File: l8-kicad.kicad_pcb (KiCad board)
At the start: 4 copper layers, 55.5 x 89.5 mm, 97 parts, among them J1 USB_B_Mini, J2 LCD 3.2" 240x320 Conn_01x14_P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, J3 Screw_Terminal_01x06, J4 Conn_ST_STDC14, J7 TC2030 - TAG Connect, Q1 SI2301CDS-T1-GE3, Q4 SI2301CDS-T1-GE3, Q5 SI2301CDS-T1-GE3, SW1 SW_Push, SW2 SW_Push, U1 B0505S-1WR2, U2 ISO1042-Q1, U22 TLV76733DRVx, U3 STM32F427V_G-I_Tx, U4 ST_SENSOR_2, U5 IIS3DHHCTR, X1 8MHz 20pF

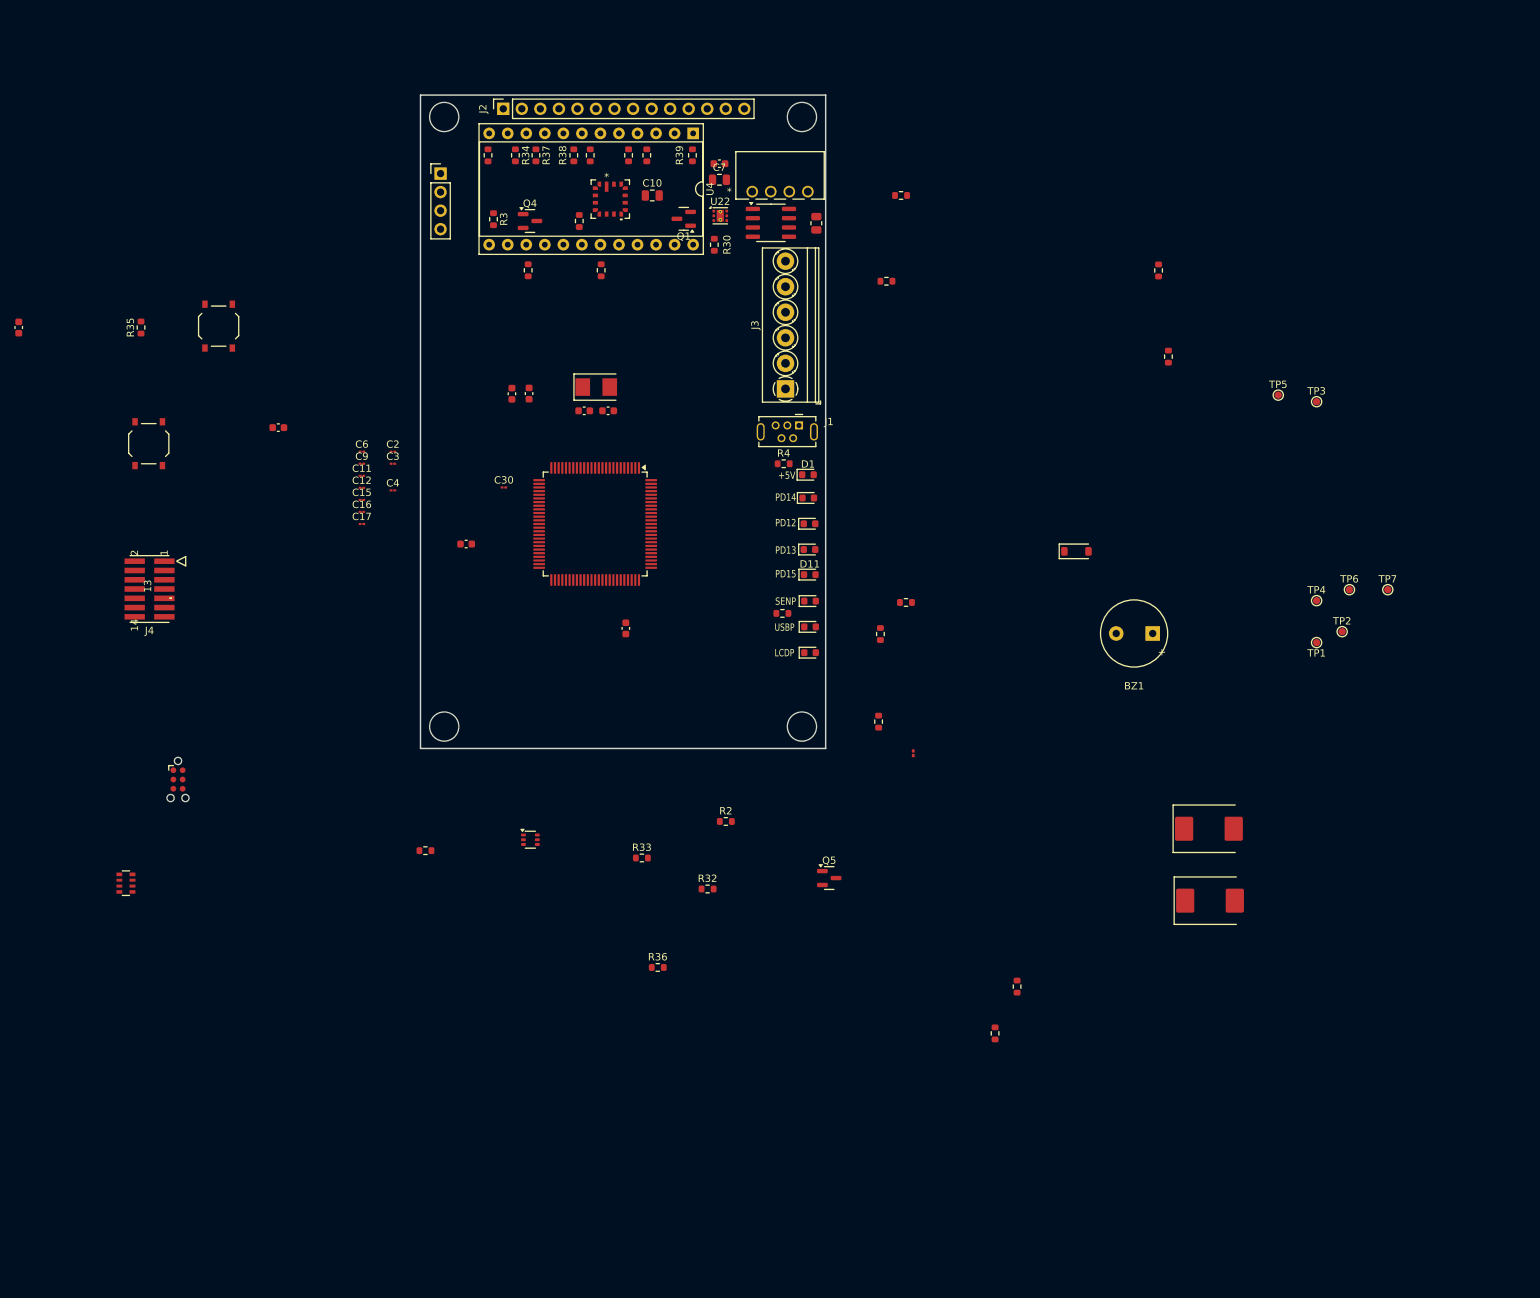
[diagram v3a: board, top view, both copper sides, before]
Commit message: add tp  move leds +
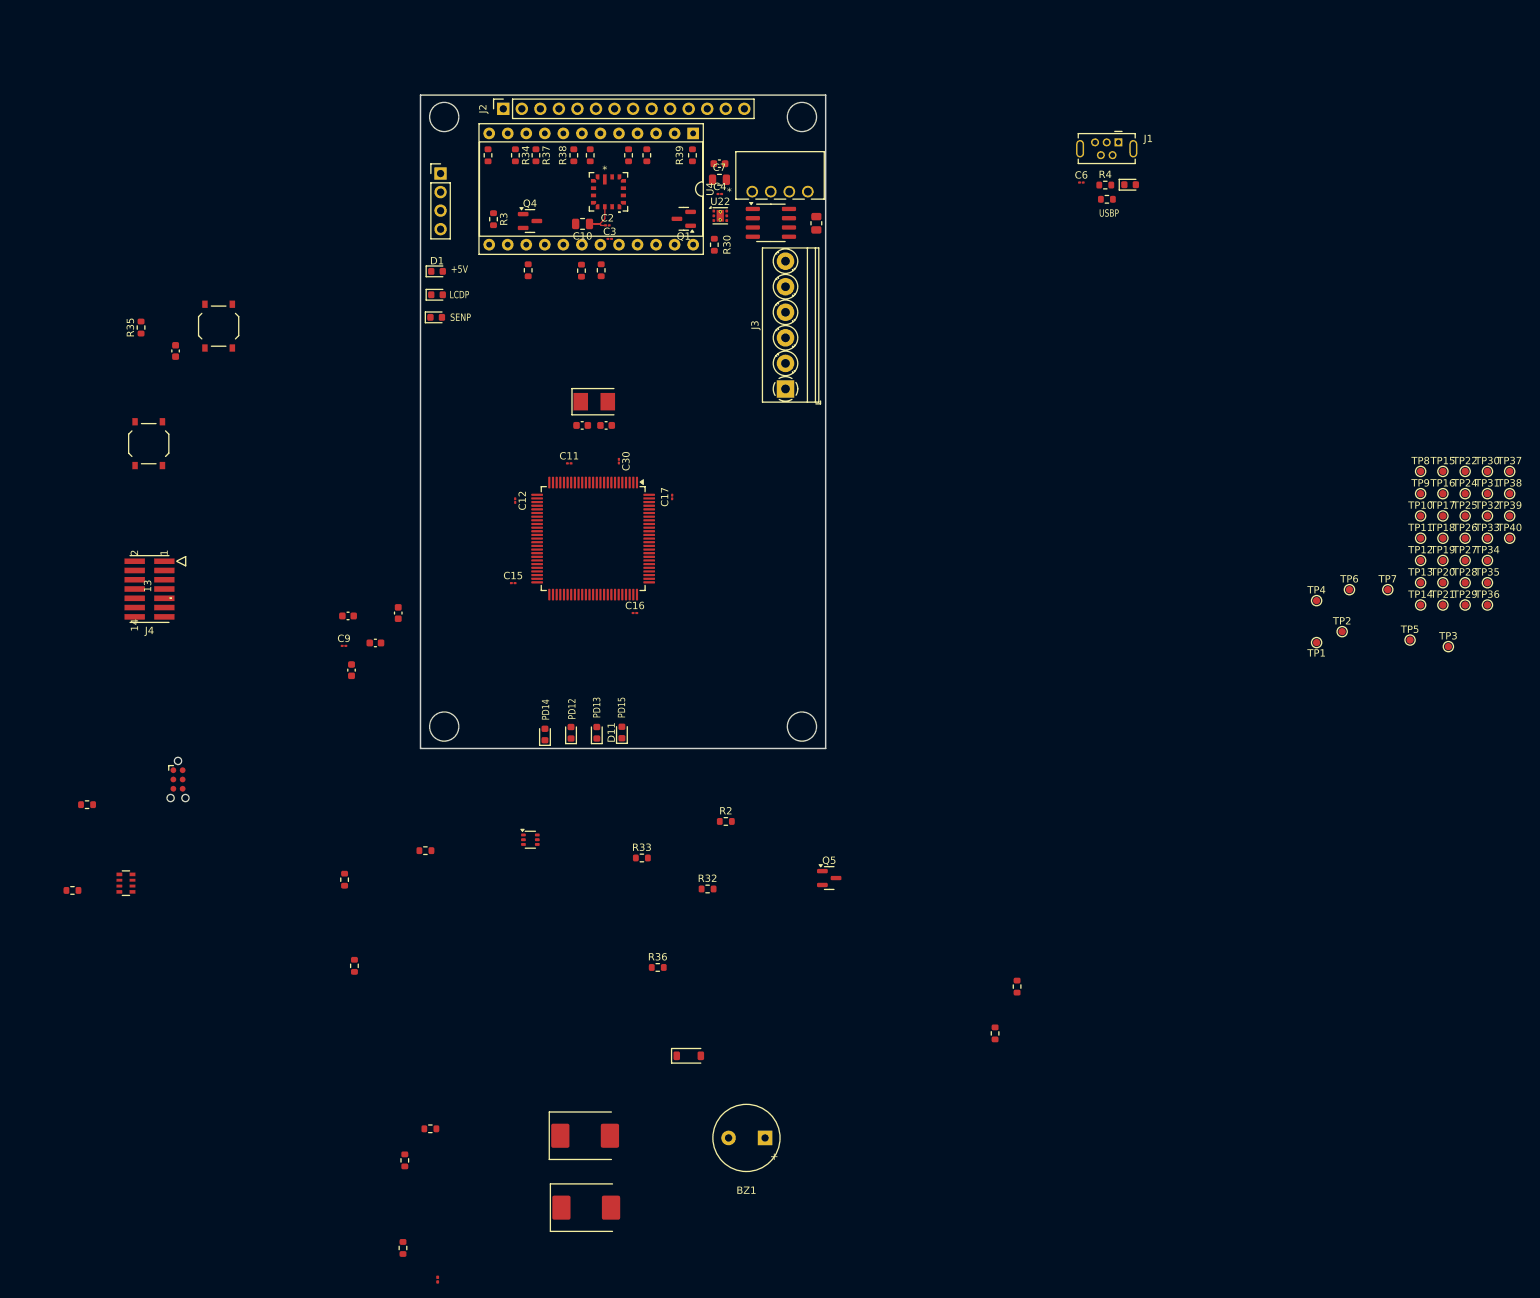
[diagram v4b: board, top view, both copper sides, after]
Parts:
- removed C27: 1uF, Capacitor_SMD:C_0603_1608Metric
- added TP10: PC8, TestPoint:TestPoint_Pad_D1.0mm, F.Cu at (237.0, 157.7)
- added TP11: PC9, TestPoint:TestPoint_Pad_D1.0mm, F.Cu at (237.0, 160.7)
- added TP12: PC13, TestPoint:TestPoint_Pad_D1.0mm, F.Cu at (237.0, 163.8)
- added TP13: PC14, TestPoint:TestPoint_Pad_D1.0mm, F.Cu at (237.0, 166.8)
- added TP14: PC15, TestPoint:TestPoint_Pad_D1.0mm, F.Cu at (237.0, 169.8)
- added TP15: PC0, TestPoint:TestPoint_Pad_D1.0mm, F.Cu at (240.1, 151.6)
- added TP16: PA0, TestPoint:TestPoint_Pad_D1.0mm, F.Cu at (240.1, 154.6)
- added TP17: PA1, TestPoint:TestPoint_Pad_D1.0mm, F.Cu at (240.1, 157.7)
- added TP18: PA4, TestPoint:TestPoint_Pad_D1.0mm, F.Cu at (240.1, 160.7)
- added TP19: PA8, TestPoint:TestPoint_Pad_D1.0mm, F.Cu at (240.1, 163.8)
- added TP20: PB4, TestPoint:TestPoint_Pad_D1.0mm, F.Cu at (240.1, 166.8)
- added TP21: PB5, TestPoint:TestPoint_Pad_D1.0mm, F.Cu at (240.1, 169.8)
- added TP22: PB8, TestPoint:TestPoint_Pad_D1.0mm, F.Cu at (243.1, 151.6)
- added TP24: PB10, TestPoint:TestPoint_Pad_D1.0mm, F.Cu at (243.1, 154.6)
- added TP25: PB11, TestPoint:TestPoint_Pad_D1.0mm, F.Cu at (243.1, 157.7)
- added TP26: PB12, TestPoint:TestPoint_Pad_D1.0mm, F.Cu at (243.1, 160.7)
- added TP27: PD6, TestPoint:TestPoint_Pad_D1.0mm, F.Cu at (243.1, 163.8)
- added TP28: PD7, TestPoint:TestPoint_Pad_D1.0mm, F.Cu at (243.1, 166.8)
- added TP29: PD8, TestPoint:TestPoint_Pad_D1.0mm, F.Cu at (243.1, 169.8)
- added TP30: PD9, TestPoint:TestPoint_Pad_D1.0mm, F.Cu at (246.2, 151.6)
- added TP31: PE8, TestPoint:TestPoint_Pad_D1.0mm, F.Cu at (246.2, 154.6)
- added TP32: PE7, TestPoint:TestPoint_Pad_D1.0mm, F.Cu at (246.2, 157.7)
- added TP33: PE0, TestPoint:TestPoint_Pad_D1.0mm, F.Cu at (246.2, 160.7)
- added TP34: PE1, TestPoint:TestPoint_Pad_D1.0mm, F.Cu at (246.2, 163.8)
- added TP35: PE9, TestPoint:TestPoint_Pad_D1.0mm, F.Cu at (246.2, 166.8)
- added TP36: PE10, TestPoint:TestPoint_Pad_D1.0mm, F.Cu at (246.2, 169.8)
- added TP37: PE11, TestPoint:TestPoint_Pad_D1.0mm, F.Cu at (249.2, 151.6)
- added TP38: PE12, TestPoint:TestPoint_Pad_D1.0mm, F.Cu at (249.2, 154.6)
- added TP39: PD10, TestPoint:TestPoint_Pad_D1.0mm, F.Cu at (249.2, 157.7)
- added TP40: PD11, TestPoint:TestPoint_Pad_D1.0mm, F.Cu at (249.2, 160.7)
- added TP8: PC6, TestPoint:TestPoint_Pad_D1.0mm, F.Cu at (237.0, 151.6)
- added TP9: PC7, TestPoint:TestPoint_Pad_D1.0mm, F.Cu at (237.0, 154.6)
- moved R13 139.3 mm to (91.0, 219.3)
- moved R45 139.3 mm to (52.3, 208.9)
- moved R47 139.3 mm to (54.3, 197.2)
- moved R5 139.3 mm to (89.6, 207.5)
- moved C6 105.2 mm to (190.5, 112.0)
- moved R43 97.2 mm to (97.8, 245.9)
- moved R8 97.2 mm to (97.6, 257.9)
- moved FB1 97.2 mm to (102.3, 262.3)
- moved R6 97.2 mm to (101.3, 241.6)
- moved D2 95.2 mm to (122.5, 242.6)
- moved D3 95.2 mm to (122.7, 252.4)
- moved BZ1 87.1 mm to (148.4, 242.8)
- moved D17 87.1 mm to (136.8, 231.6)
- moved D10 74.8 mm to (197.2, 112.3)
- moved R48 72.1 mm to (194.0, 114.3)
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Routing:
- net +3.3V: track 0.00 -> 5.73 mm

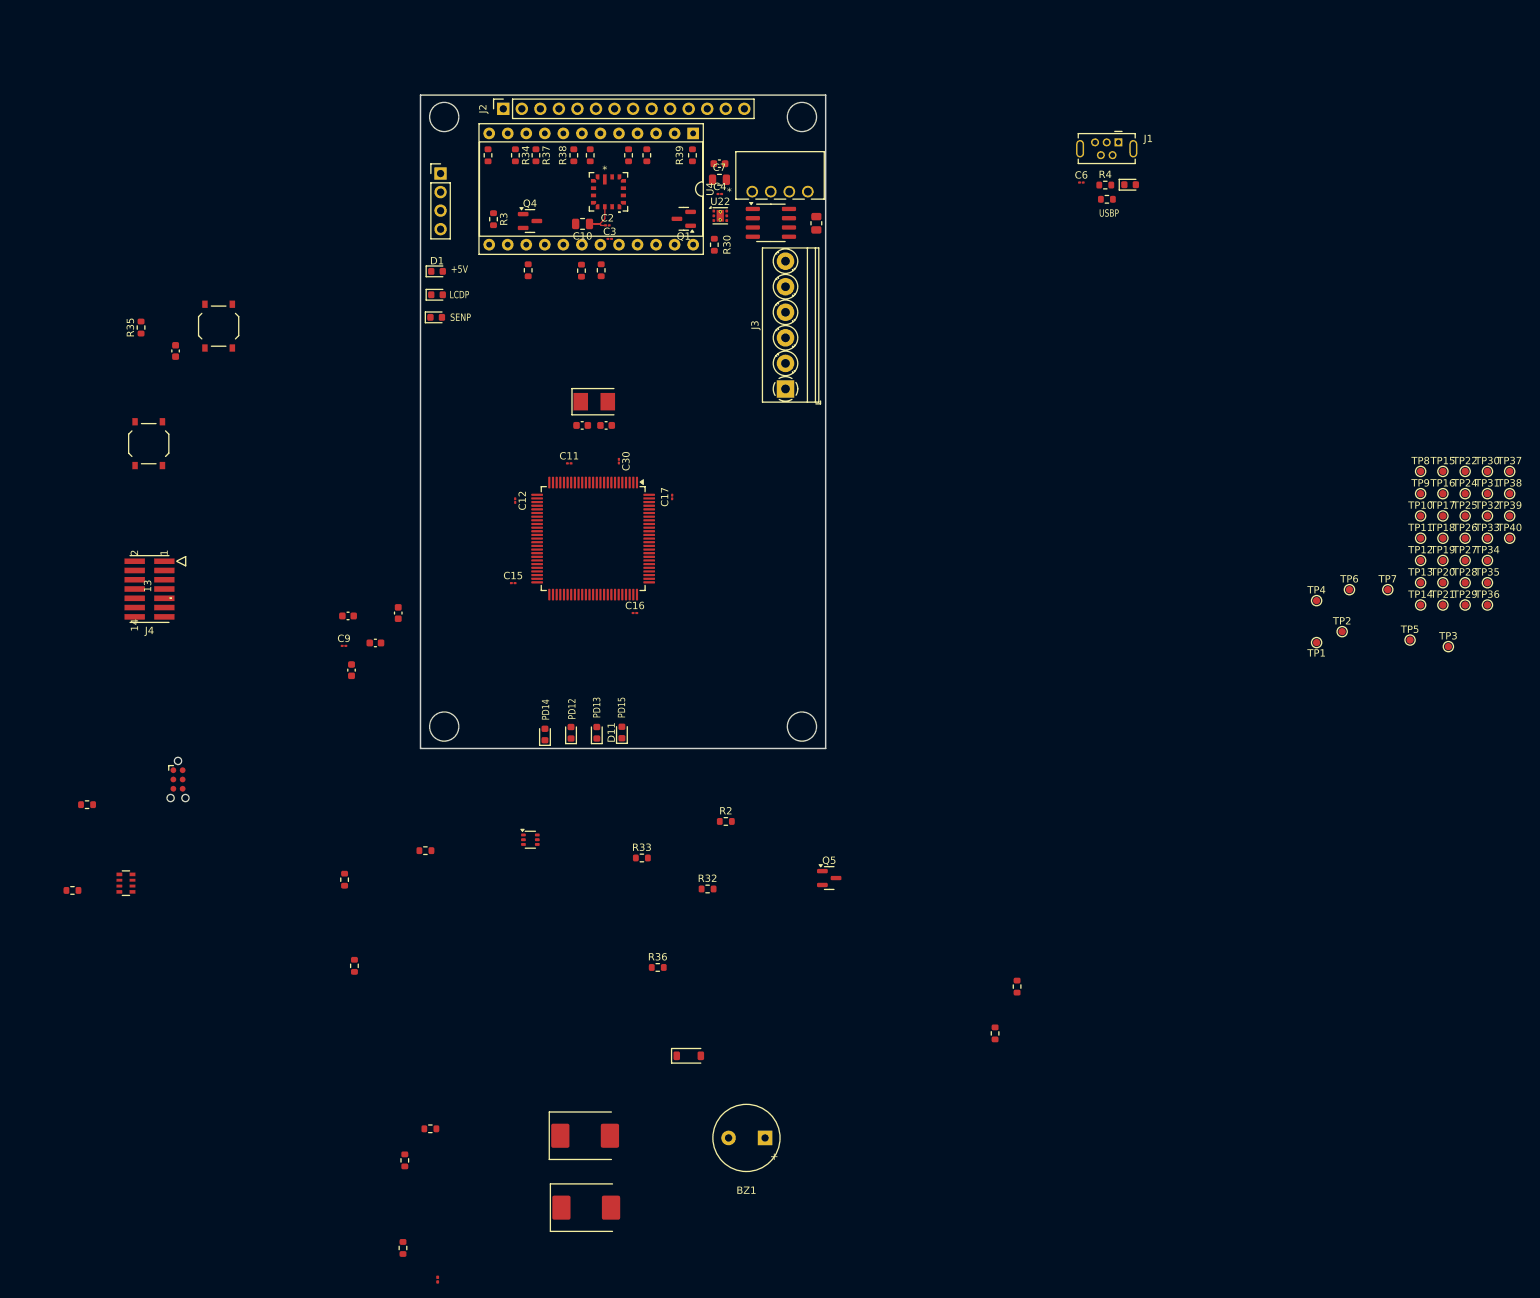
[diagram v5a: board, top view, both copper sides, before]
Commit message: smaller test pads
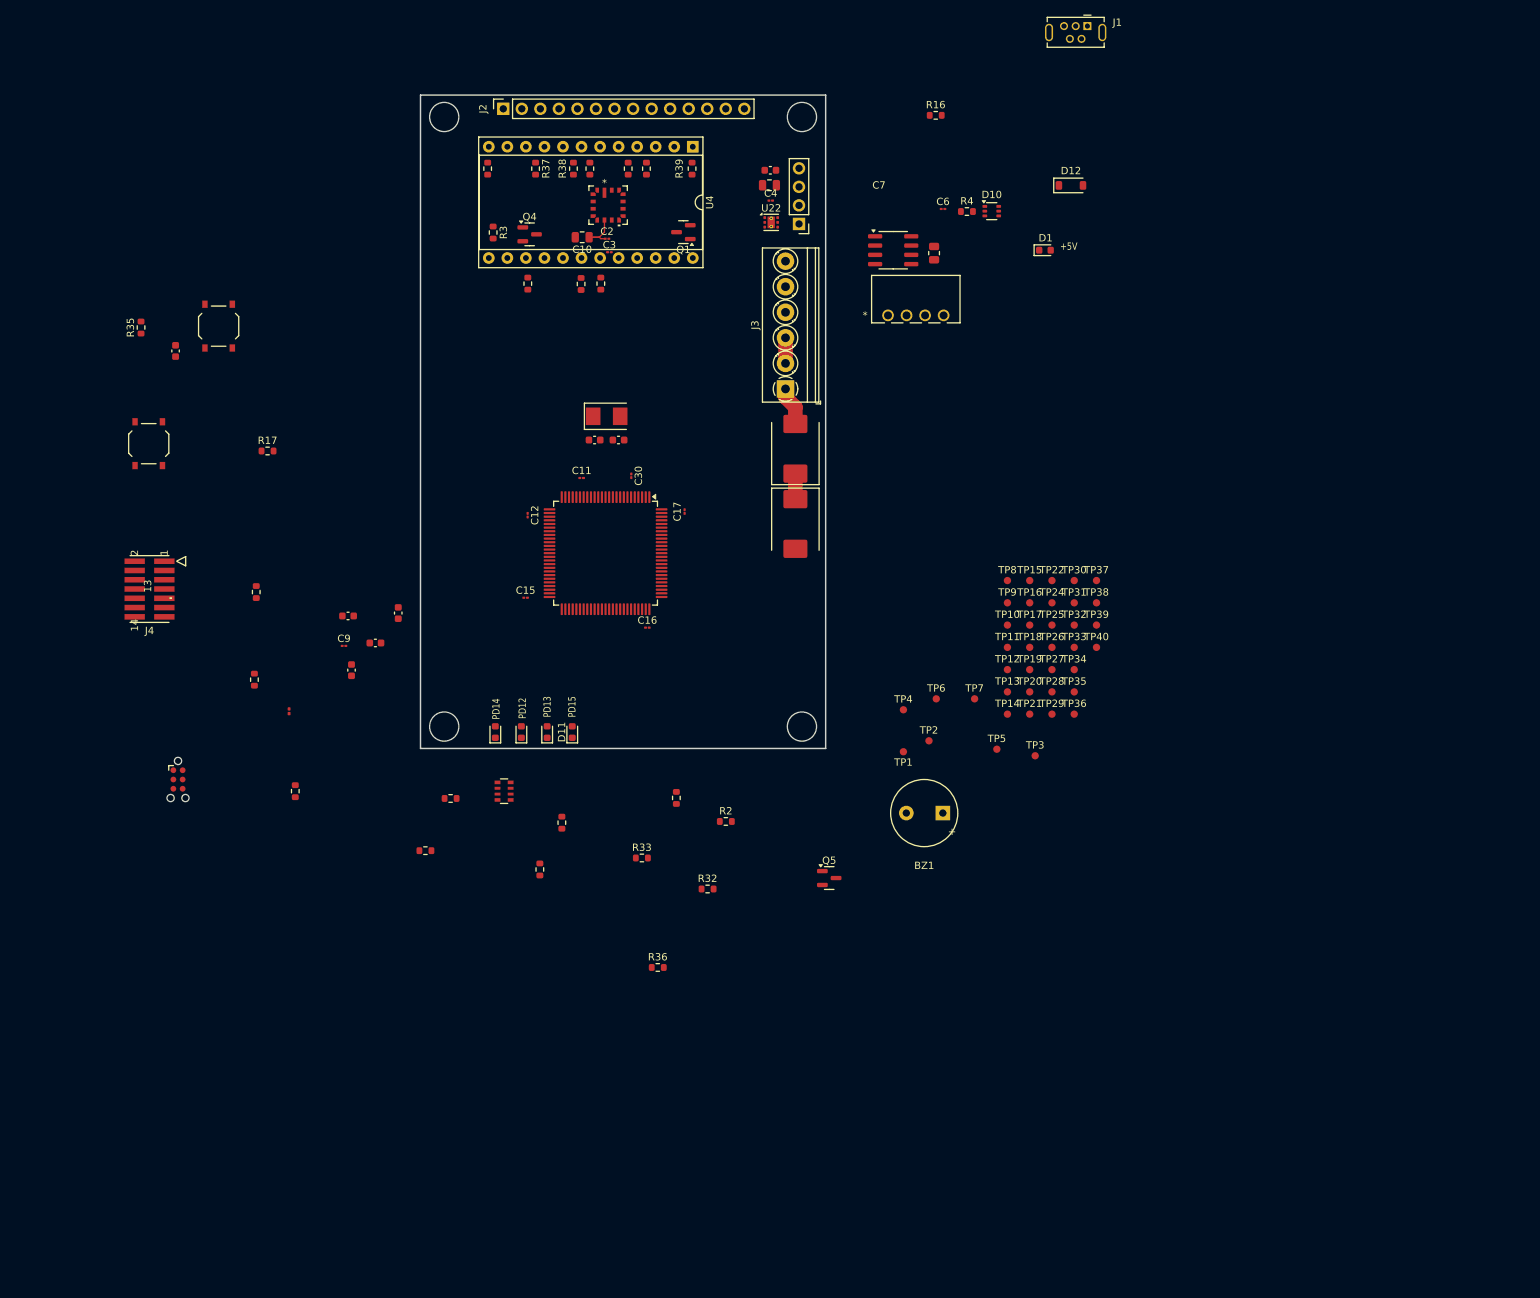
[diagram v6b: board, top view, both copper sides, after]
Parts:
- removed D16: SRV05-4, Package_TO_SOT_SMD:SOT-363_SC-70-6
- removed D17: B5819W, Diode_SMD:D_SOD-123
- removed D8, D9: LED-YELLOW, LED_SMD:LED_0603_1608Metric
- removed R30: 100R, Resistor_SMD:R_0603_1608Metric
- removed R34: 1k, Resistor_SMD:R_0603_1608Metric
- removed R47: 100K, Resistor_SMD:R_0603_1608Metric
- removed R48: 1K, Resistor_SMD:R_0603_1608Metric
- removed R6: 2.2K, Resistor_SMD:R_0603_1608Metric
- added D12: B5819W, Diode_SMD:D_SOD-123, F.Cu at (189.1, 112.4)
- added R16: 10K, Resistor_SMD:R_0603_1608Metric, F.Cu at (170.6, 102.8)
- added R17: 2.2K, Resistor_SMD:R_0603_1608Metric, F.Cu at (79.0, 148.8)
- D10: value LED-YELLOW -> SRV05-4; footprint LED_SMD:LED_0603_1608Metric -> Package_TO_SOT_SMD:SOT-363_SC-70-6
- D3: value SM15T33C -> SM15T100CA
- R13: value R100 -> 100R
- R5: value 10K -> 100K
- TP1, TP10, TP11, TP12, TP13, TP14, TP15, TP16, TP17, TP18, TP19, TP2, TP20, TP21, TP22, TP24, TP25, TP26, TP27, TP28, TP29, TP3, TP30, TP31, TP32, TP33, TP34, TP35, TP36, TP37, TP38, TP39, TP4, TP40, TP5, TP6, TP7, TP8, TP9: footprint TestPoint:TestPoint_Pad_D1.0mm -> dnt:TestPoint_Pad_D1.0mm FP .6R
- moved D2 98.4 mm to (151.3, 148.4), turned to 90 degrees
- moved D3 97.9 mm to (151.3, 158.8), turned to -90 degrees
- moved D1 83.3 mm to (185.5, 121.2)
- moved R43 80.5 mm to (77.5, 168.1)
- moved R8 80.5 mm to (77.2, 180.1)
- moved FB1 80.5 mm to (82.0, 184.4)
- moved R10 66.3 mm to (119.4, 199.7)
- moved R9 66.3 mm to (116.3, 206.1)
- moved TP16 58.5 mm to (183.4, 169.6)
- moved TP18 58.5 mm to (183.4, 175.7)
- moved TP21 58.5 mm to (183.4, 184.8)
- moved TP15 58.5 mm to (183.4, 166.5)
- moved TP17 58.5 mm to (183.4, 172.6)
- moved TP19 58.5 mm to (183.4, 178.7)
- moved TP20 58.5 mm to (183.4, 181.8)
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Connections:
- C6 pad 1: /MCU/Shield -> /usb/Shield
- D10 pad 1: Net-(D10-K) -> /PA10
- D10 pad 2: Net-(D10-A) -> GND
- J1 pad 1: Net-(D10-A) -> Net-(D12-A)
- J1 pad 2: /MCU/USB_OTG_FS_DM -> /USB_OTG_FS_DM
- J1 pad 3: /MCU/USB_OTG_FS_DP -> /USB_OTG_FS_DP
- J1 pad 4: /MCU/PA10 -> /PA10
- J1 pad 6: /MCU/Shield -> /usb/Shield
- J3 pad 1: GND -> /VBATT
- J3 pad 3: /VBATT -> GND
- R5 pad 1: Net-(D10-A) -> /usb/Shield
- R5 pad 2: /MCU/USB_OTG_FS_VBUS -> GND
- U3 pad 68: /MCU/USB_OTG_FS_VBUS -> /USB_OTG_FS_VBUS
- U3 pad 69: /MCU/PA10 -> /PA10
- U3 pad 70: /MCU/USB_OTG_FS_DM -> /USB_OTG_FS_DM
- U3 pad 71: /MCU/USB_OTG_FS_DP -> /USB_OTG_FS_DP
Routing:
- net /VBATT: track 0.00 -> 6.21 mm
- net Net-(D1-A): track 0.00 -> 3.50 mm
- net GND: track 0.00 -> 3.50 mm
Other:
- board text removed: "LCDP"
- board text removed: "SENP"
- board text removed: "USBP"
